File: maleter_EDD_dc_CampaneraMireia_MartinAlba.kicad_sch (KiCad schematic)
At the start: 0 parts

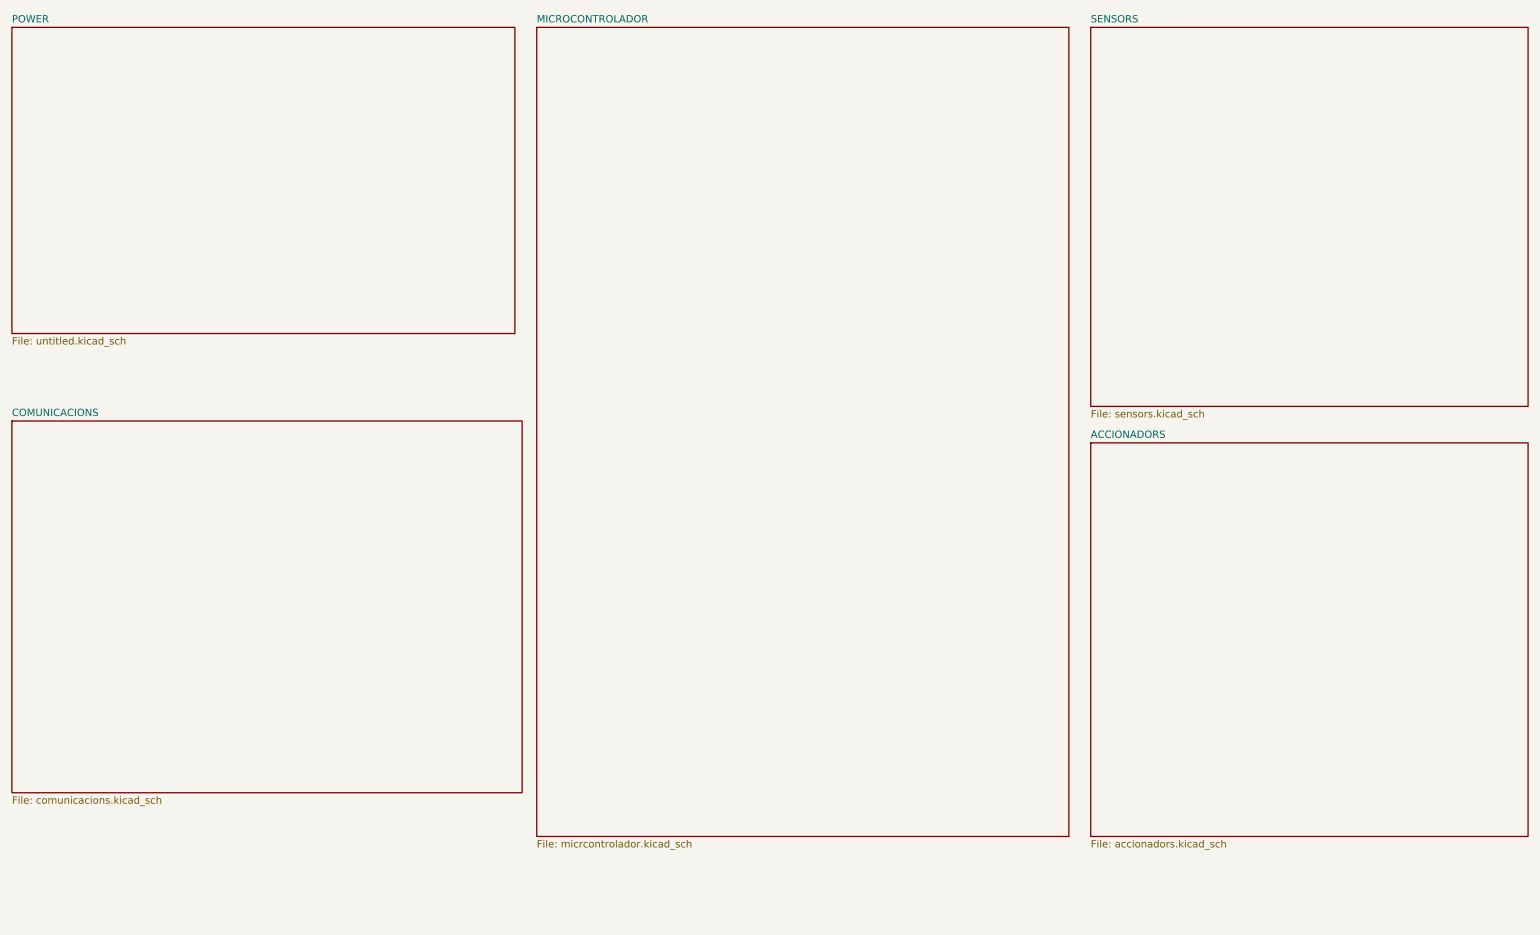
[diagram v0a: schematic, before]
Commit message: Actualització projecte KiCad
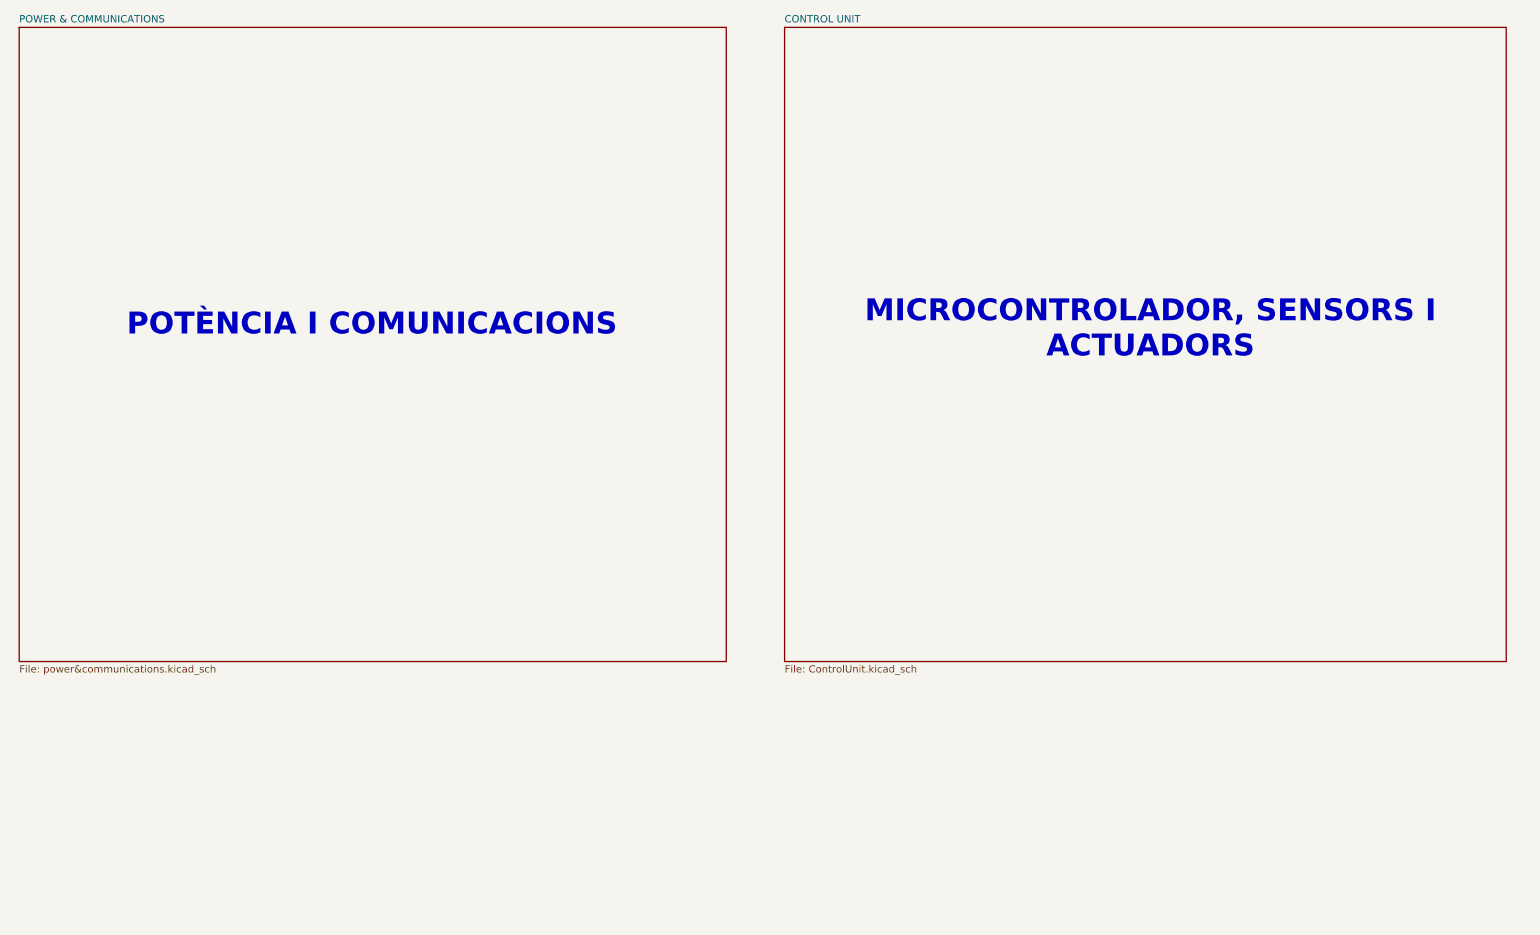
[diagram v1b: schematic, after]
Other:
- removed sheet ACCIONADORS
- removed sheet COMUNICACIONS
- removed sheet MICROCONTROLADOR
- removed sheet POWER
- removed sheet SENSORS
- added sheet CONTROL UNIT (ControlUnit.kicad_sch)
- added sheet POWER & COMMUNICATIONS (power&communications.kicad_sch)
- note added: "MICROCONTROLADOR, SENSORS I ACTUADORS"
- note added: "POTÈNCIA I COMUNICACIONS"
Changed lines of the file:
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@@
 	(generator_version "9.0")
 	(paper "A4")
+	(text "POTÈNCIA I COMUNICACIONS\n"
+		(exclude_from_sim no)
+		(at 79.248 68.326 0)
+		(effects
+			(font
+				(size 3.81 3.81)
+				(thickness 1.016)
+				(bold yes)
+			)
+		)
+	)
+	(text "MICROCONTROLADOR, SENSORS I \nACTUADORS"
+		(exclude_from_sim no)
+		(at 214.884 69.088 0)
+		(effects
+			(font
+				(size 3.81 3.81)
+				(thickness 1.016)
+				(bold yes)
+			)
+		)
+	)
 	(sheet
-		(at 16.51 85.09)
-		(size 88.9 64.77)
+		(at 151.13 16.51)
+		(size 125.73 110.49)
 		(exclude_from_sim no)
 		(in_bom yes)
@@
 			(color 0 0 0 0.0000)
 		)
-		(property "Sheetname" "COMUNICACIONS"
-			(at 16.51 84.3784 0)
+		(property "Sheetname" "CONTROL UNIT"
+			(at 151.13 15.7984 0)
 			(effects
 				(font
@@
 			)
 		)
-		(property "Sheetfile" "comunicacions.kicad_sch"
-			(at 16.51 150.4446 0)
+		(property "Sheetfile" "ControlUnit.kicad_sch"
+			(at 151.13 127.5846 0)
 			(effects
 				(font
@@
 	)
 	(sheet
-		(at 16.51 16.51)
-		(size 87.63 53.34)
+		(at 17.78 16.51)
+		(size 123.19 110.49)
 		(exclude_from_sim no)
 		(in_bom yes)
@@
 			(color 0 0 0 0.0000)
 		)
-		(property "Sheetname" "POWER"
-			(at 16.51 15.7984 0)
+		(property "Sheetname" "POWER & COMMUNICATIONS"
+			(at 17.78 15.7984 0)
 			(effects
 				(font
@@
 			)
 		)
-		(property "Sheetfile" "untitled.kicad_sch"
-			(at 16.51 70.4346 0)
+		(property "Sheetfile" "power&communications.kicad_sch"
+			(at 17.78 127.5846 0)
 			(effects
 				(font
@@
 			(project "maleter_EDD_dc_CampaneraMireia_MartinAlba"
 				(path "/c2b694d2-752b-44f8-812f-8731bb340544"
-					(page "2")
+					(page "4")
 				)
 			)
-		)
-	)
-	(sheet
-		(at 107.95 16.51)
-		(size 92.71 140.97)
-		(exclude_from_sim no)
-		(in_bom yes)
-		(on_board yes)
-		(dnp no)
-		(fields_autoplaced yes)
-		(stroke
-			(width 0.1524)
-			(type solid)
-		)
-		(fill
-			(color 0 0 0 0.0000)
-		)
-		(property "Sheetname" "MICROCONTROLADOR"
-			(at 107.95 15.7984 0)
-			(effects
-				(font
-					(size 1.27 1.27)
-				)
-				(justify left bottom)
-			)
-		)
-		(property "Sheetfile" "micrcontrolador.kicad_sch"
-			(at 107.95 158.0646 0)
-			(effects
-				(font
-					(size 1.27 1.27)
-				)
-				(justify left top)
-			)
-		)
-		(instances
-			(project "maleter_EDD_dc_CampaneraMireia_MartinAlba"
-				(path "/c2b694d2-752b-44f8-812f-8731bb340544"
-					(page "3")
-				)
-			)
-		)
-	)
-	(sheet
-		(at 204.47 88.9)
-		(size 76.2 68.58)
-		(exclude_from_sim no)
-		(in_bom yes)
-		(on_board yes)
-		(dnp no)
-		(fields_autoplaced yes)
-		(stroke
-			(width 0.1524)
-			(type solid)
-		)
-		(fill
-			(color 0 0 0 0.0000)
-		)
-		(property "Sheetname" "ACCIONADORS"
-			(at 204.47 88.1884 0)
-			(effects
-				(font
-					(size 1.27 1.27)
-				)
-				(justify left bottom)
-			)
-		)
-		(property "Sheetfile" "accionadors.kicad_sch"
-			(at 204.47 158.0646 0)
-			(effects
-				(font
-					(size 1.27 1.27)
-				)
-				(justify left top)
-			)
-		)
-		(instances
-			(project "maleter_EDD_dc_CampaneraMireia_MartinAlba"
-				(path "/c2b694d2-752b-44f8-812f-8731bb340544"
-					(page "6")
-				)
-			)
-		)
-	)
-	(sheet
-		(at 204.47 16.51)
-		(size 76.2 66.04)
-		(exclude_from_sim no)
-		(in_bom yes)
-		(on_board yes)
-		(dnp no)
-		(fields_autoplaced yes)
-		(stroke
-			(width 0.1524)
-			(type solid)
-		)
-		(fill
-			(color 0 0 0 0.0000)
-		)
-		(property "Sheetname" "SENSORS"
-			(at 204.47 15.7984 0)
-			(effects
-				(font
-					(size 1.27 1.27)
-				)
-				(justify left bottom)
-			)
-		)
-		(property "Sheetfile" "sensors.kicad_sch"
-			(at 204.47 83.1346 0)
-			(effects
-				(font
-					(size 1.27 1.27)
-				)
-				(justify left top)
-			)
-		)
-		(instances
-			(project "maleter_EDD_dc_CampaneraMireia_MartinAlba"
-				(path "/c2b694d2-752b-44f8-812f-8731bb340544"
-					(page "5")
-				)
-			)

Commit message: Correccions professor
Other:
- note added: "MIREIA CAMPANERA I ALBA MARTÍN PROJECTE MALETER EDD"
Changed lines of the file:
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@@
 	(generator_version "9.0")
 	(paper "A4")
+	(text "MIREIA CAMPANERA I ALBA MARTÍN\nPROJECTE MALETER EDD"
+		(exclude_from_sim no)
+		(at 178.562 170.434 0)
+		(effects
+			(font
+				(size 1.27 1.27)
+			)
+			(justify left)
+		)
+	)
 	(text "POTÈNCIA I COMUNICACIONS\n"
 		(exclude_from_sim no)

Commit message: Ultima versio projecte
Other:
- sheet POWER & COMMUNICATIONS renamed ALIMENTACIO I MOTOR
- note added: "ALIMENTACIÓ I MOTOR"
- note added: "MICROCONTROLADOR, SENSORS I COMUNICACIONS"
- note removed: "MICROCONTROLADOR, SENSORS I ACTUADORS"
- note removed: "POTÈNCIA I COMUNICACIONS"
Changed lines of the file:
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@@
 		)
 	)
-	(text "POTÈNCIA I COMUNICACIONS\n"
+	(text "ALIMENTACIÓ I MOTOR\n"
 		(exclude_from_sim no)
 		(at 79.248 68.326 0)
@@
 		)
 	)
-	(text "MICROCONTROLADOR, SENSORS I \nACTUADORS"
+	(text "MICROCONTROLADOR, SENSORS I \nCOMUNICACIONS"
 		(exclude_from_sim no)
 		(at 214.884 69.088 0)
@@
 			(color 0 0 0 0.0000)
 		)
-		(property "Sheetname" "POWER & COMMUNICATIONS"
+		(property "Sheetname" "ALIMENTACIO I MOTOR"
 			(at 17.78 15.7984 0)
 			(effects
